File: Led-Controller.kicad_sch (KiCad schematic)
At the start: 43 parts, among them J1 Barrel_Jack, J2 Screw_Terminal, Q1 CSD18540Q5B, Q2 CSD18540Q5B, Q3 CSD18540Q5B, Q4 CSD18540Q5B, Q5 CSD18540Q5B, U1 AMS1117-5.0, U2 AMS1117-3.3, U3 1ED44175N01BXTSA1, U4 1ED44175N01BXTSA1, U5 1ED44175N01BXTSA1, U6 1ED44175N01BXTSA1, U7 1ED44175N01BXTSA1, U8 ESP32-WROOM-32E

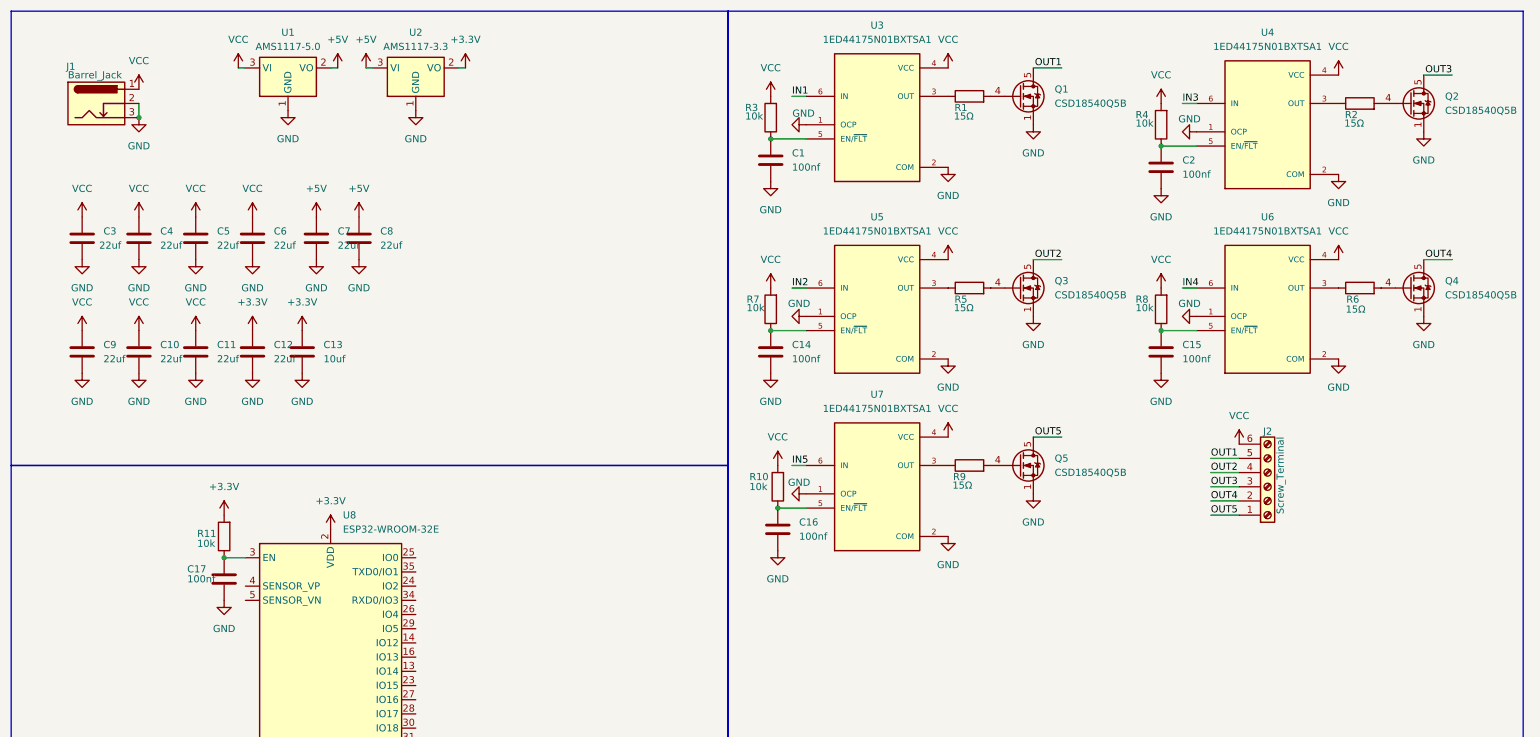
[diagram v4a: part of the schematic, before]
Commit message: Added: Reverse voltage protection (#19)
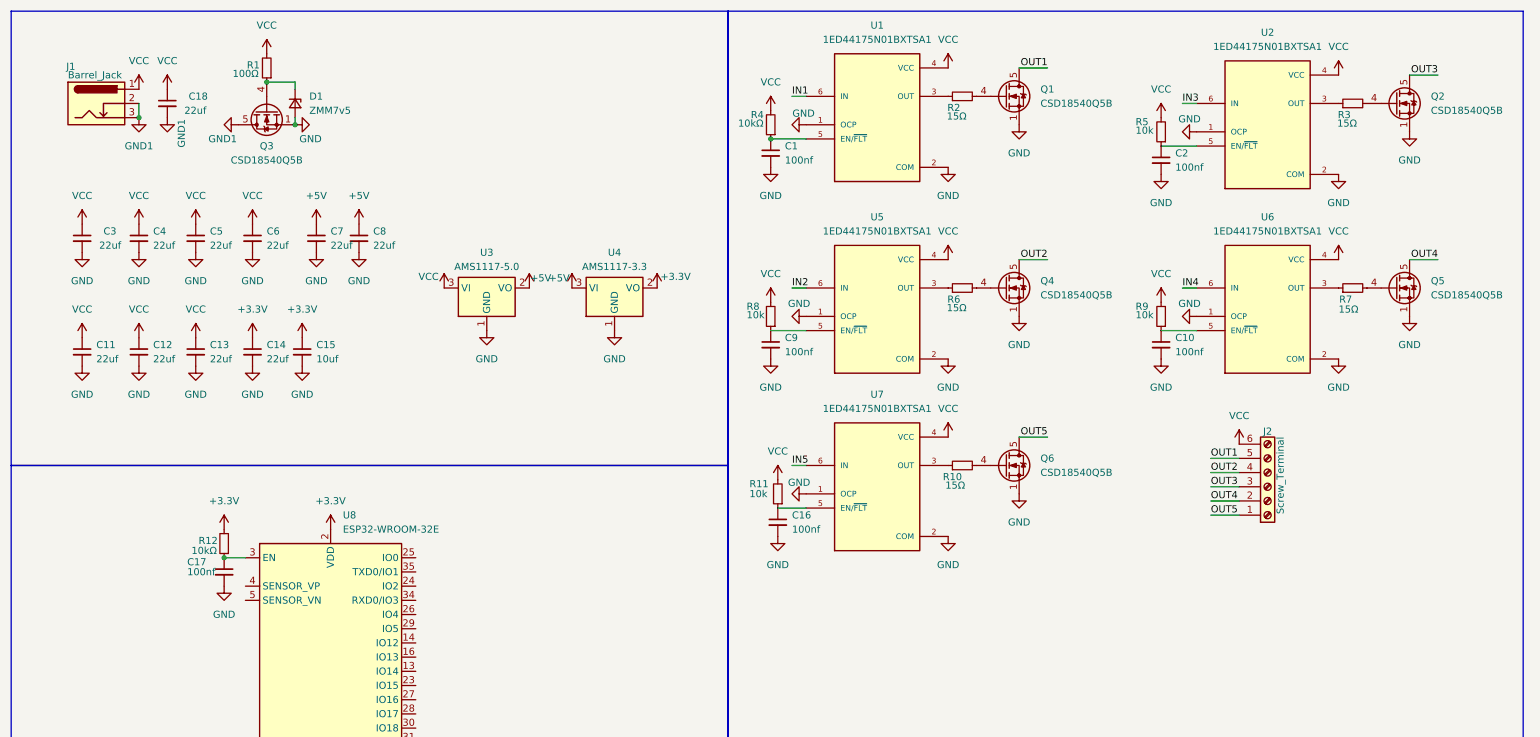
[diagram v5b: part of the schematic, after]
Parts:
- added C18: 22uf, Capacitor_SMD:C_0805_2012Metric_Pad1.18x1.45mm_HandSolder, symbol Device:C_Small
- added D1: ZMM7v5, Diode_SMD:D_MiniMELF, symbol Device:D_Zener_Small
- added Q3: CSD18540Q5B, Package_TO_SOT_SMD:TDSON-8-1, symbol Transistor_FET:CSD18540Q5B
- added R1: 100Ω, Resistor_SMD:R_0402_1005Metric, symbol Device:R_Small
- C1, C16, C17, C2, C3, C4, C5, C6, C7, C8: symbol Device:C -> Device:C_Small
- C10: renamed from C15; symbol Device:C -> Device:C_Small
- C11: renamed from C9; symbol Device:C -> Device:C_Small
- C12: renamed from C10; symbol Device:C -> Device:C_Small
- C13: renamed from C11; symbol Device:C -> Device:C_Small
- C14: renamed from C12; symbol Device:C -> Device:C_Small
- C15: renamed from C13; symbol Device:C -> Device:C_Small
- C9: renamed from C14; symbol Device:C -> Device:C_Small
- R10: renamed from R9; symbol Device:R -> Device:R_Small
- R11: renamed from R10; symbol Device:R -> Device:R_Small
- R12: renamed from R11; value 10k -> 10kΩ; symbol Device:R -> Device:R_Small
- R2: renamed from R1; symbol Device:R -> Device:R_Small
- R3: renamed from R2; symbol Device:R -> Device:R_Small
- R4: renamed from R3; value 10k -> 10kΩ; symbol Device:R -> Device:R_Small
- R5: renamed from R4; symbol Device:R -> Device:R_Small
- R6: renamed from R5; symbol Device:R -> Device:R_Small
- R7: renamed from R6; symbol Device:R -> Device:R_Small
- R8: renamed from R7; symbol Device:R -> Device:R_Small
- R9: renamed from R8; symbol Device:R -> Device:R_Small
- renumbered Q3 to Q4, Q4 to Q5, Q5 to Q6, U3 to U1, U4 to U2, U1 to U3, U2 to U4
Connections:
- net GND: now also D1.2 (A), Q3.1 (S), Q3.2 (S), Q3.3 (S); no longer J1.2, J1.3
- net VCC: now also C18.1, R1.2
- new net: D1.1 (K), Q3.4 (G), R1.1
- new net GND1: C18.2, J1.2, J1.3, Q3.5 (D)
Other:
- moved on the sheet: C1, C10, C16, C17, C2, C9, Q1, Q2, Q4, Q5, Q6, R10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

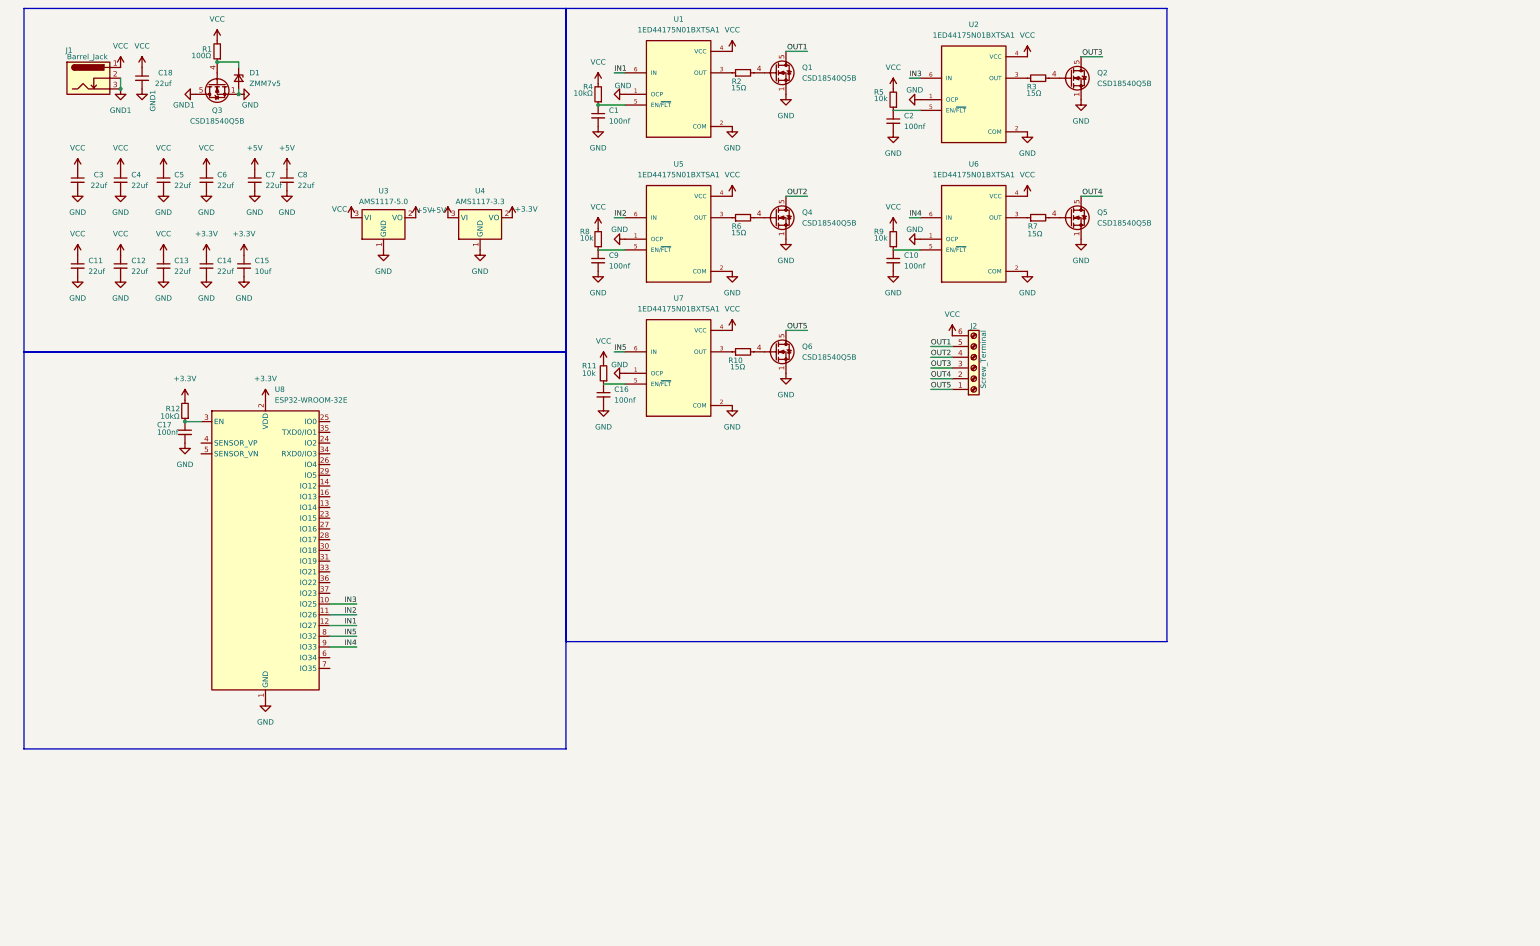
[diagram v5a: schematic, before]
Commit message: Added: 6 Pin IDC Connector for Programming (#20)
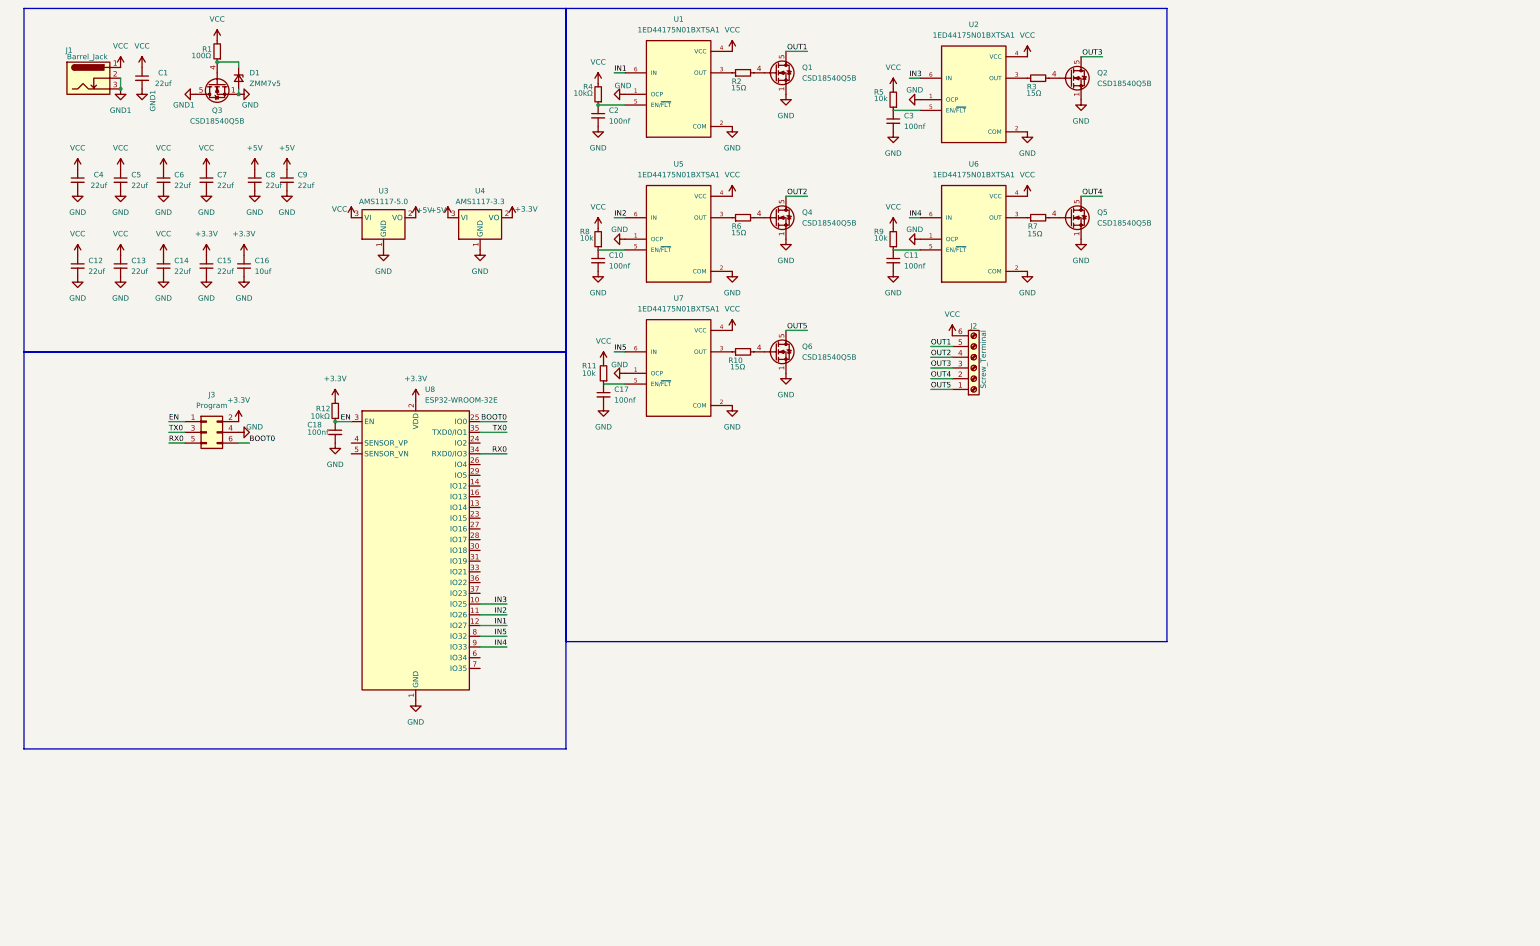
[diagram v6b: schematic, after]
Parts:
- added J3: Program, Connector_PinHeader_1.27mm:PinHeader_2x03_P1.27mm_Vertical, symbol Connector_Generic:Conn_02x03_Odd_Even
- renumbered C18 to C1, C9 to C10, C10 to C11, C11 to C12, C12 to C13, C13 to C14, C14 to C15, C15 to C16, C16 to C17, C17 to C18, C1 to C2, C2 to C3, C3 to C4, C4 to C5, C5 to C6, C6 to C7, C7 to C8, C8 to C9
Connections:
- net +3.3V: now also J3.2 (Pin_2)
- net GND: now also J3.4 (Pin_4)
- net EN: now reaches C18.1, R12.1, U8.3 (EN)
- net EN: now also J3.1 (Pin_1)
- net BOOT0: now reaches U8.25 (IO0)
- net BOOT0: now also J3.6 (Pin_6)
- net RX0: now reaches U8.34 (RXD0/IO3)
- net RX0: now also J3.5 (Pin_5)
- net TX0: now reaches U8.35 (TXD0/IO1)
- net TX0: now also J3.3 (Pin_3)
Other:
- moved on the sheet: C18, R12, U8

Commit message: Added: Switching Regulator (#21)
* Added: Switching Regulator Schematic

* Added: Final Layout for the Switching regulator along with the overall PCB layout
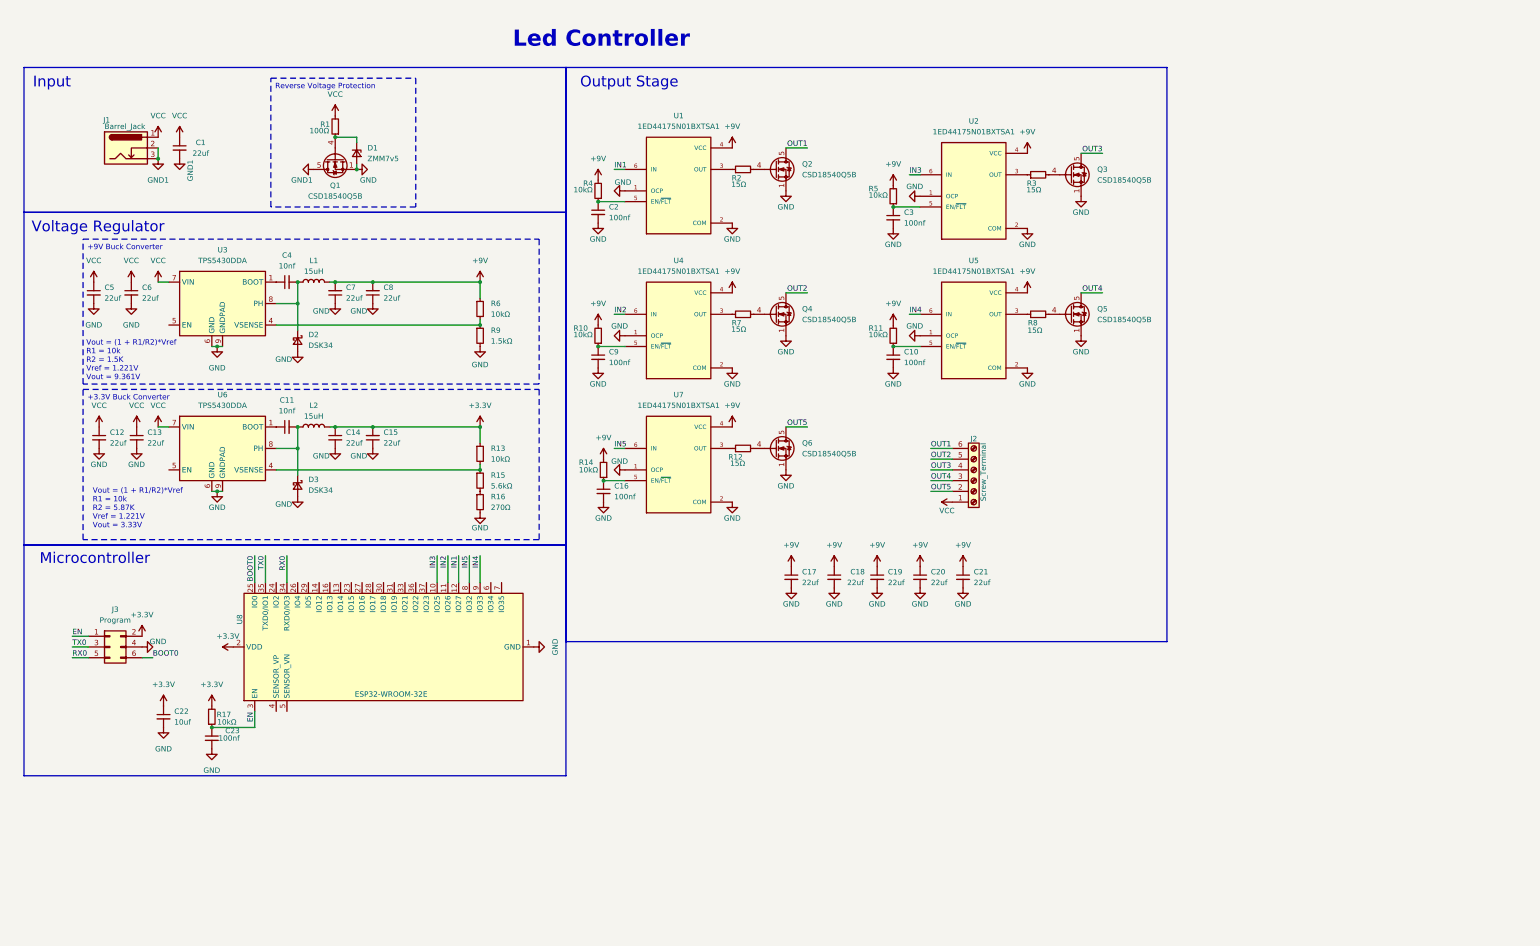
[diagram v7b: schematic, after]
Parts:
- removed C9: 22uf, Capacitor_SMD:C_0805_2012Metric_Pad1.18x1.45mm_HandSolder, symbol Device:C_Small
- removed U3: AMS1117-5.0, Package_TO_SOT_SMD:SOT-223-3_TabPin2, symbol Regulator_Linear:AMS1117-5.0
- removed U4: AMS1117-3.3, Package_TO_SOT_SMD:SOT-223-3_TabPin2, symbol Regulator_Linear:AMS1117-5.0
- added C11, C4: 10nf, Capacitor_SMD:C_0402_1005Metric, symbol Device:C_Small
- added C12, C5: 22uf, Capacitor_SMD:C_0805_2012Metric_Pad1.18x1.45mm_HandSolder, symbol Device:C_Small
- added C15, C7: 22uf, Capacitor_SMD:C_0805_2012Metric, symbol Device:C_Small
- added D2, D3: DSK34, Diode_SMD:D_SOD-123, symbol Device:D_Schottky_Small
- added L1, L2: 15uH, Inductor_SMD:L_Bourns-SRN8040_8x8.15mm, symbol Device:L
- added R13, R6: 10kΩ, Resistor_SMD:R_0402_1005Metric, symbol Device:R_Small
- added R15: 5.6kΩ, Resistor_SMD:R_0402_1005Metric, symbol Device:R_Small
- added R16: 270Ω, Resistor_SMD:R_0402_1005Metric, symbol Device:R_Small
- added R9: 1.5kΩ, Resistor_SMD:R_0402_1005Metric, symbol Device:R_Small
- added U3, U6: TPS5430DDA, Package_SO:TI_SO-PowerPAD-8_ThermalVias, symbol Regulator_Switching:TPS5430DDA
- C14: renamed from C15; footprint Capacitor_SMD:C_0805_2012Metric_Pad1.18x1.45mm_HandSolder -> Capacitor_SMD:C_0805_2012Metric
- C8: footprint Capacitor_SMD:C_0805_2012Metric_Pad1.18x1.45mm_HandSolder -> Capacitor_SMD:C_0805_2012Metric
- R10: renamed from R8; value 10k -> 10kΩ
- R11: renamed from R9; value 10k -> 10kΩ
- R14: renamed from R11; value 10k -> 10kΩ
- R5: value 10k -> 10kΩ
- renumbered C11 to C10, C14 to C13, C17 to C16, C12 to C17, C4 to C18, C5 to C19, C6 to C20, C7 to C21, C16 to C22, C18 to C23, C13 to C6, C10 to C9, Q3 to Q1, Q1 to Q2, Q2 to Q3, R10 to R12, R12 to R17, R6 to R7, R7 to R8, U5 to U4, U6 to U5
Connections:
- net +5V is gone; now on net GND: C8.1
- net +3.3V: now also C15.2, L2.2, R13.1
- net GND: now also C12.2, C15.1, C5.2, C7.1, D2.2 (A), D3.2 (A), R16.2, R9.2, U3.6 (GND), U3.9 (GNDPAD), U6.6 (GND), U6.9 (GNDPAD); no longer C8.2
- net OUT1: now also J2.6 (Pin_6); no longer J2.5 (Pin_5)
- net OUT2: now also J2.5 (Pin_5); no longer J2.4 (Pin_4)
- net OUT3: now also J2.4 (Pin_4); no longer J2.3 (Pin_3)
- net OUT4: now also J2.3 (Pin_3); no longer J2.2 (Pin_2)
- net OUT5: now also J2.2 (Pin_2); no longer J2.1 (Pin_1)
- net VCC: now also J2.1 (Pin_1), C12.1, C5.1, U3.7 (VIN), U6.7 (VIN); no longer C17.1, C18.1, C19.1, C20.1, C21.1, J2.6 (Pin_6), R10.2, R11.2, R14.2, R4.2, R5.2, U1.4 (VCC), U2.4 (VCC), U4.4 (VCC), U5.4 (VCC), U7.4 (VCC)
- new net: R6.2, R9.1, U3.4 (VSENSE)
- new net: R13.2, R15.1, U6.4 (VSENSE)
- new net: C11.1, U6.1 (BOOT)
- new net: C11.2, D3.1 (K), L2.1, U6.8 (PH)
- new net: R15.2, R16.1
- new net: C4.1, U3.1 (BOOT)
- new net: C4.2, D2.1 (K), L1.1, U3.8 (PH)
- new net +9V: C17.1, C18.1, C19.1, C20.1, C21.1, C7.2, C8.2, L1.2, R10.2, R11.2, R14.2, R4.2, R5.2, R6.1, U1.4 (VCC), U2.4 (VCC), U4.4 (VCC), U5.4 (VCC), U7.4 (VCC)
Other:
- note added: "Input"
- note added: "Led Controller"
- note added: "Microcontroller"
- note added: "Output Stage"
- note added: "Voltage Regulator"
- note added: "Vout = (1 + R1/R2)*Vref R1 = 10k R2 = 1.5K Vref = 1.221V Vout = 9.361V"
- note added: "Vout = (1 + R1/R2)*Vref R1 = 10k R2 = 5.87K Vref = 1.221V Vout = 3.33V"
- title: (none) -> LightWave
- moved on the sheet: C1, C10, C13, C14, C16, C17, C18, C19, C2, C20, C21, C22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
